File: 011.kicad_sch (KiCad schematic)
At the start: 25 parts, among them Q1 CJ2101, Q2 CJ2101, U1 AM6232ASCGHAALWR

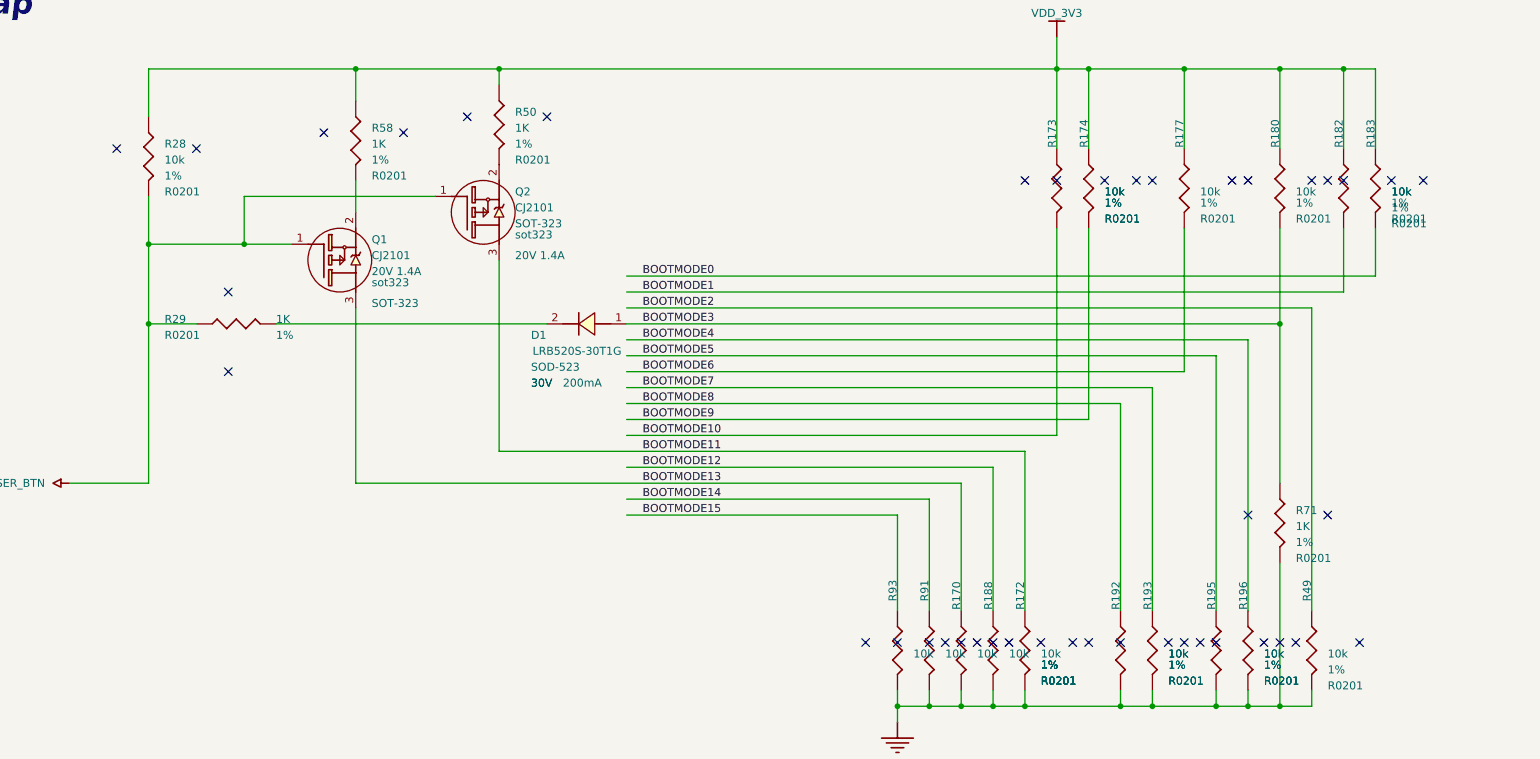
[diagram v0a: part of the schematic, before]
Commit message: Remove rando NCs added during conversion
Also a little tidying.

TODO: check junctions that may be missing. Noticed a few obvious ones
and corrected them already.

Signed-off-by: Michael Welling <mwelling79@gmail.com>
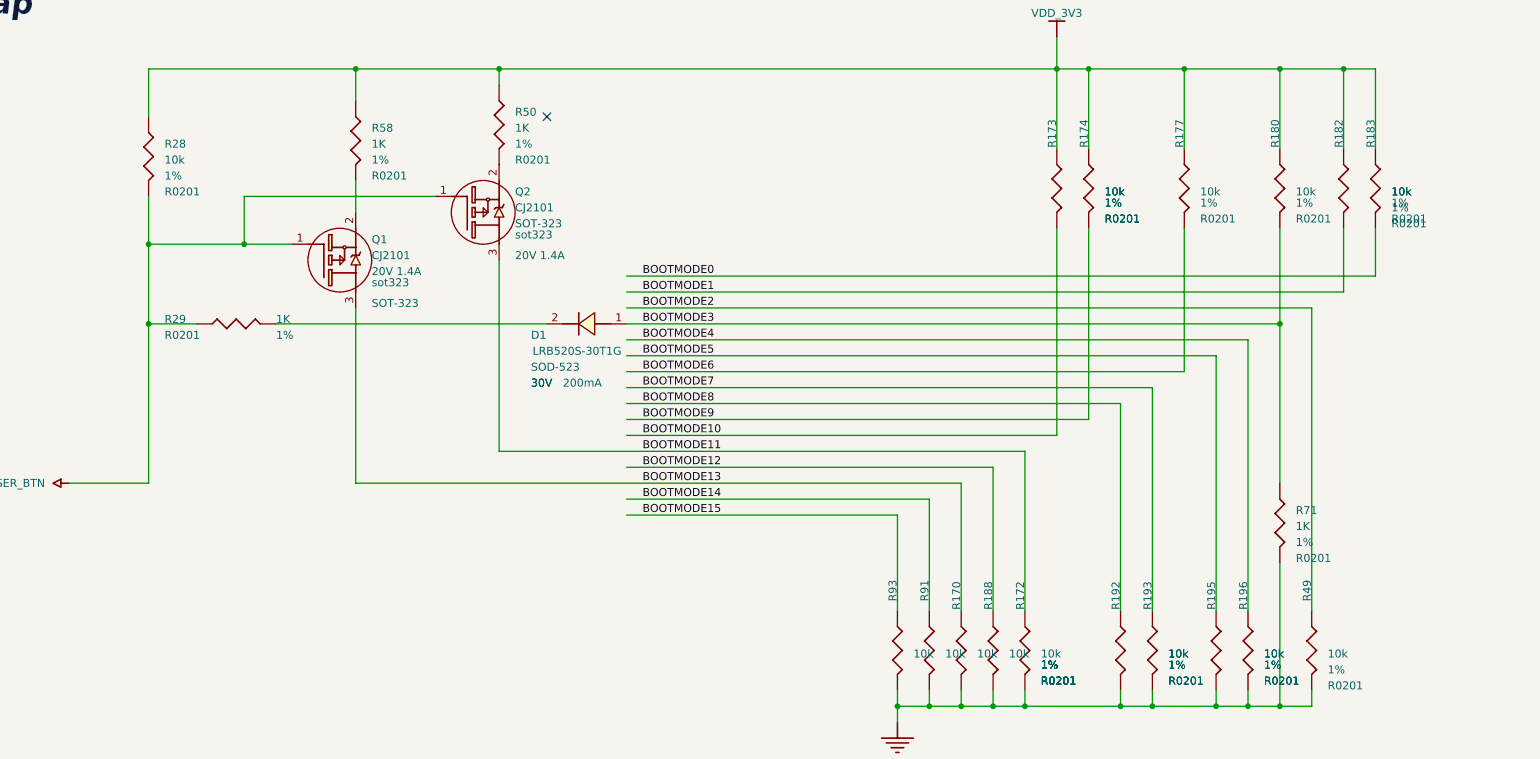
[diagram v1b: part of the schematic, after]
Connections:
- no-connect marks 52 -> 11
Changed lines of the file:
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@@
-	)
-	(no_connect
-		(at 210.82 261.62)
-	)
-	(no_connect
-		(at 195.58 261.62)
-	)
-	(no_connect
-		(at 185.42 261.62)
 	)
 	(no_connect
@@
 	)
 	(no_connect
-		(at 220.98 187.96)
-	)
-	(no_connect
-		(at 215.9 261.62)
-	)
-	(no_connect
 		(at 86.36 83.82)
-	)
-	(no_connect
-		(at 231.14 261.62)
-	)
-	(no_connect
-		(at 259.08 187.96)
-	)
-	(no_connect
-		(at 208.28 261.62)
 	)
 	(no_connect
@@
 	)
 	(no_connect
-		(at 213.36 187.96)
-	)
-	(no_connect
-		(at 218.44 187.96)
-	)
-	(no_connect
-		(at 88.9 180.34)
-	)
-	(no_connect
-		(at 264.16 187.96)
-	)
-	(no_connect
 		(at 86.36 101.6)
-	)
-	(no_connect
-		(at 193.04 261.62)
 	)
 	(no_connect
@@
 	)
 	(no_connect
-		(at 198.12 261.62)
-	)
-	(no_connect
-		(at 236.22 241.3)
-	)
-	(no_connect
-		(at 251.46 187.96)
-	)
-	(no_connect
-		(at 101.6 180.34)
-	)
-	(no_connect
-		(at 254 261.62)
-	)
-	(no_connect
-		(at 55.88 182.88)
-	)
-	(no_connect
 		(at 124.46 177.8)
-	)
-	(no_connect
-		(at 233.68 187.96)
-	)
-	(no_connect
-		(at 73.66 205.74)
 	)
 	(no_connect
@@
 	)
 	(no_connect
-		(at 246.38 187.96)
-	)
-	(no_connect
 		(at 86.36 116.84)
-	)
-	(no_connect
-		(at 190.5 261.62)
-	)
-	(no_connect
-		(at 228.6 261.62)
-	)
-	(no_connect
-		(at 68.58 182.88)
-	)
-	(no_connect
-		(at 248.92 187.96)
-	)
-	(no_connect
-		(at 238.76 261.62)
-	)
-	(no_connect
-		(at 180.34 261.62)
-	)
-	(no_connect
-		(at 226.06 261.62)
-	)
-	(no_connect
-		(at 73.66 218.44)
-	)
-	(no_connect
-		(at 243.84 261.62)
-	)
-	(no_connect
-		(at 236.22 187.96)
-	)
-	(no_connect
-		(at 187.96 261.62)
 	)
 	(no_connect
@@
 	)
 	(no_connect
-		(at 203.2 261.62)
-	)
-	(no_connect
 		(at 86.36 119.38)
-	)
-	(no_connect
-		(at 241.3 261.62)
-	)
-	(no_connect
-		(at 111.76 177.8)
-	)
-	(no_connect
-		(at 175.26 261.62)
-	)
-	(no_connect
-		(at 200.66 187.96)
 	)
 	(no_connect
 		(at 86.36 129.54)
 	)
-	(no_connect
-		(at 223.52 261.62)
-	)
-	(no_connect
-		(at 205.74 187.96)
-	)
-	(no_connect
-		(at 248.92 241.3)
-	)
 	(wire

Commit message: Another round of cleansing fire
Signed-off-by: Michael Welling <mwelling79@gmail.com>
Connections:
- no-connect marks 11 -> 10
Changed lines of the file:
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@@
-	)
-	(no_connect
-		(at 124.46 177.8)
 	)
 	(no_connect
